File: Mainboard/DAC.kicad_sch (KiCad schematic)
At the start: 40 parts, among them IC1 REF102AU_2K5, IC4 DAC8814IBDBT, U2 TL072, U5 TL074, U6 TL074, U7 ADG419BR

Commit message: cad update
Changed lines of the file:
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@@
 					(size 1.27 1.27)
 				)
+				(hide yes)
 			)
 		)
@@
 					(size 1.27 1.27)
 				)
+				(hide yes)
 			)
 		)

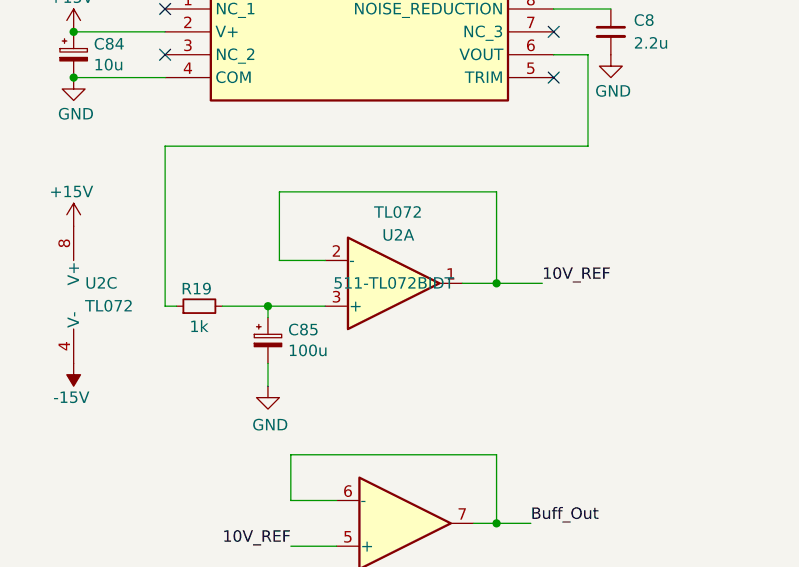
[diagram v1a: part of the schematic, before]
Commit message: updates to DAC + ADC Libraries
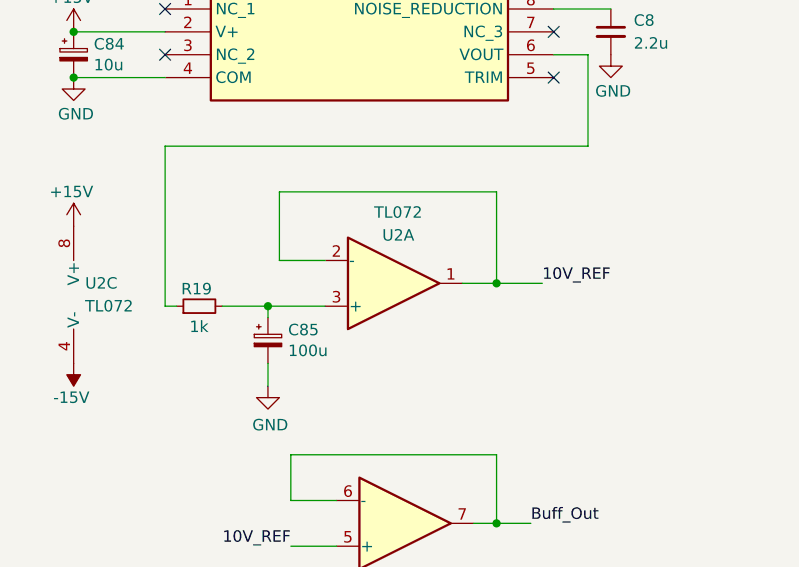
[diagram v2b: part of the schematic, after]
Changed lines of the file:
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@@
 					(size 1.27 1.27)
 				)
+				(hide yes)
 			)
 		)
